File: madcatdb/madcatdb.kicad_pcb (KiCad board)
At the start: 2 copper layers, 44 x 11 mm, 11 parts, among them J1 USB_C_Receptacle_USB2.0, J2 Conn_01x04, U1 SRV05-4

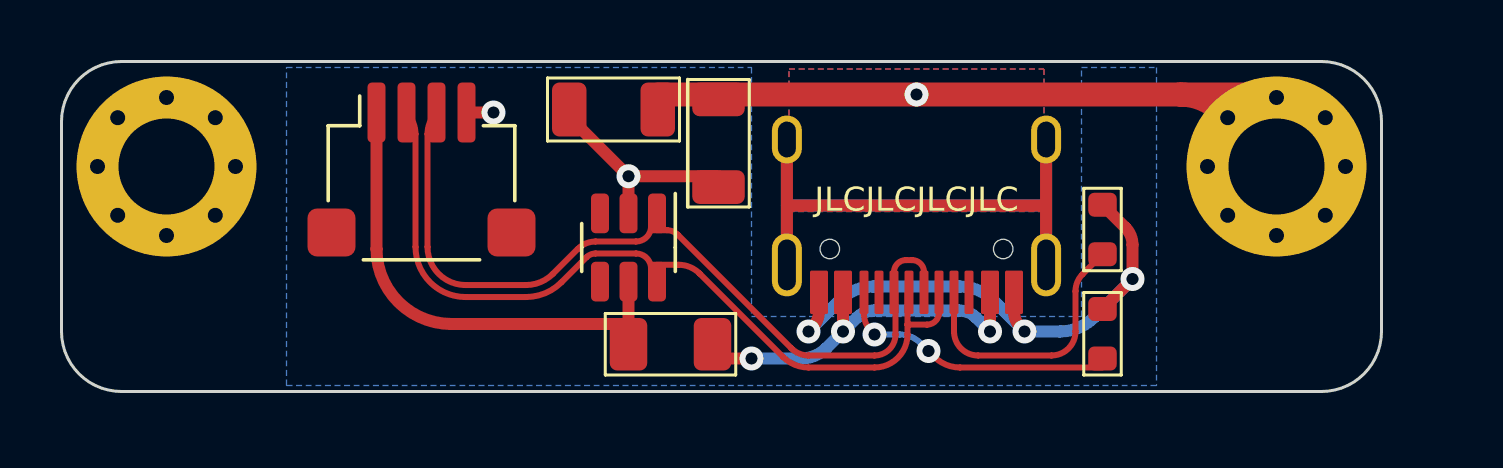
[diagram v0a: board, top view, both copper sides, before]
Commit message: updated madcat to mid mount
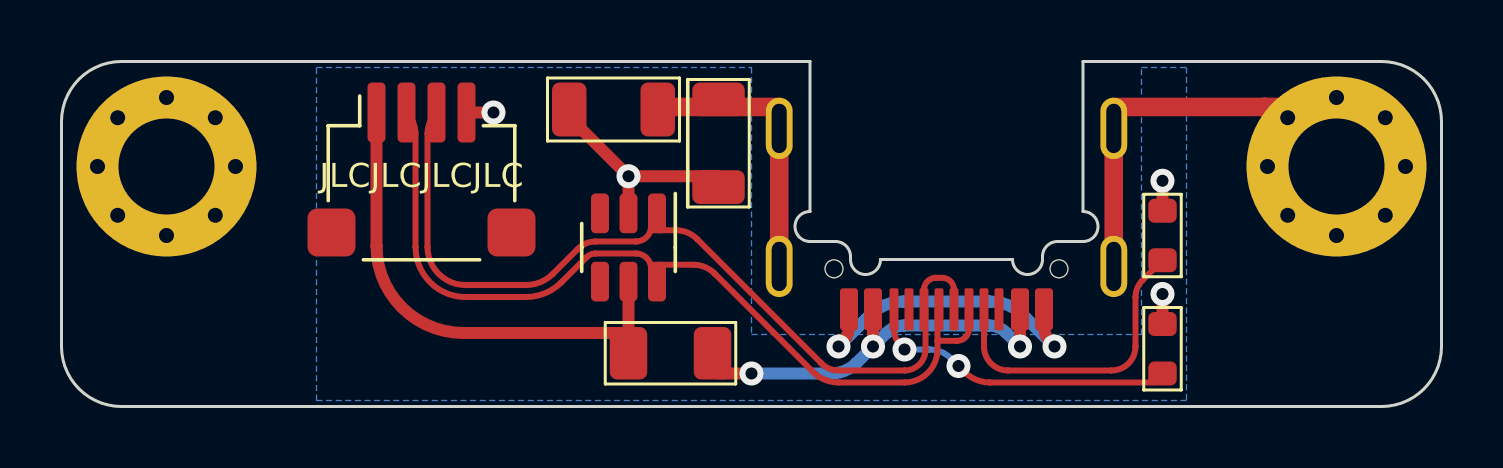
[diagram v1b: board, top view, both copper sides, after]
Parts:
- J1: footprint Crokto:USB_C_Receptacle_HRO_TYPE-C-31-M-12 -> Crokto:HRO-TYPE-C-31-M-14
- moved H3 16.5 mm to (12.0, 3.70), turned to 0 degrees
- moved R2 2.06 mm to (36.7, 9.57)
- moved R1 2.01 mm to (36.7, 5.80)
- moved H2 2.00 mm to (42.5, 3.50)
- moved J1 1.00 mm to (29.5, 3.65)
- moved F1 0.30 mm to (20.3, 9.72)
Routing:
- net Earth: track 58.8 -> 24.1 mm, vias 1 -> 0
- net GND: track 27.7 -> 21.2 mm, vias 5 -> 6
- net Net-(J1-PadA5): track 9.11 -> 10.3 mm
- net D-: track 28.1 -> 29.2 mm
- net D+: track 28.1 -> 29.1 mm
- net VBUS: track 12.8 -> 13.5 mm
- net Net-(J1-PadB5): track 9.46 -> 10.1 mm
- removed copper zone on B.Cu, net Earth
- removed copper zone on F.Cu, net Earth
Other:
- board size 44 x 11 mm -> 46 x 11.5 mm
